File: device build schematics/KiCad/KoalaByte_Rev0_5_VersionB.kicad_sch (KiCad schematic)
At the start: 0 parts

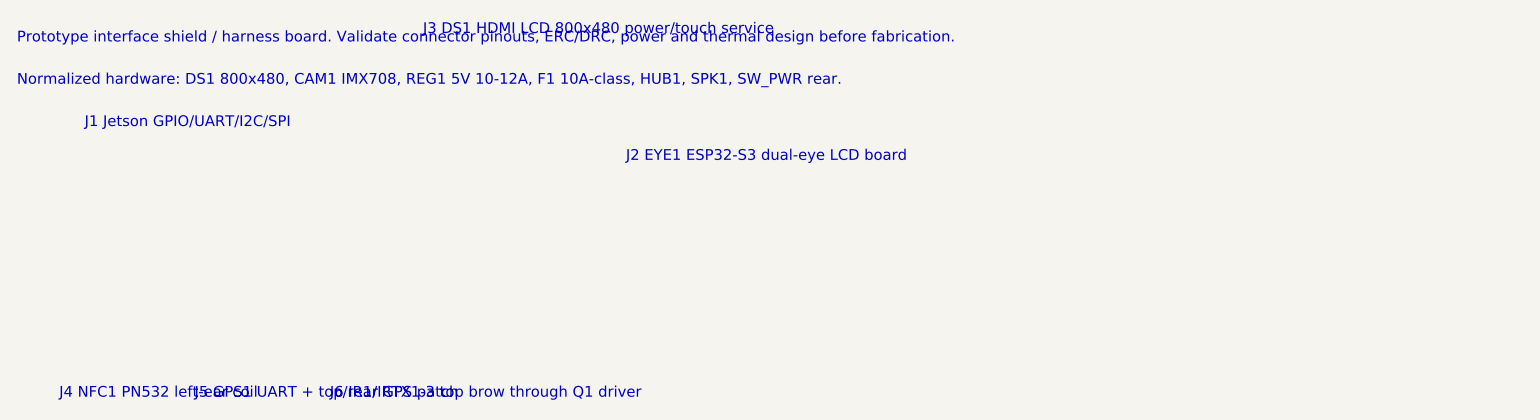
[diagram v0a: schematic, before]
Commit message: Add MIC1 schematic starter annotation
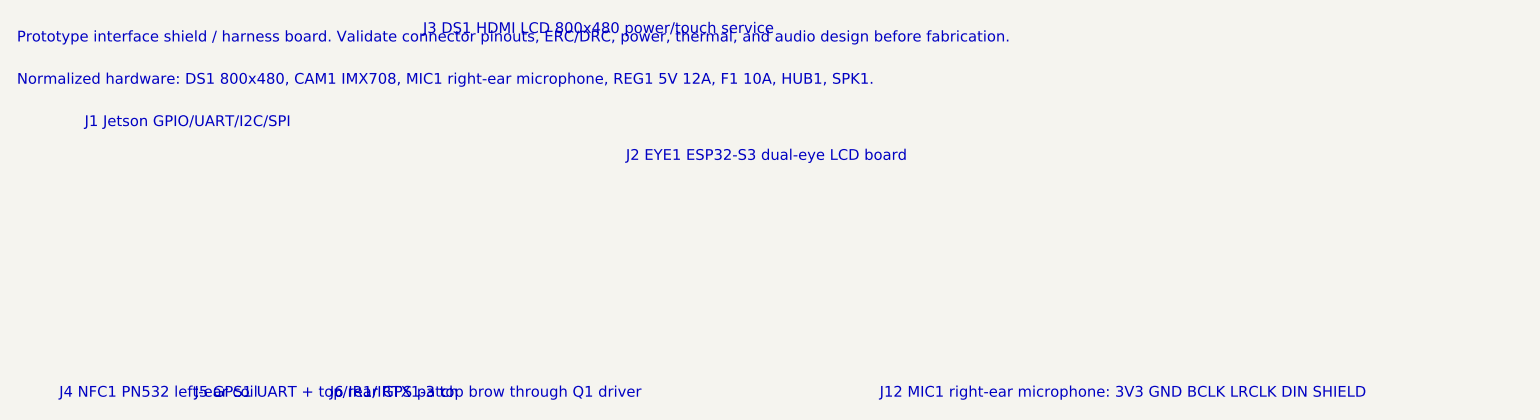
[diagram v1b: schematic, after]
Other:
- note added: "J12 MIC1 right-ear microphone: 3V3 GND BCLK LRCLK DIN SHIELD"
- note added: "Normalized hardware: DS1 800x480, CAM1 IMX708, MIC1 right-ear microphone, REG1 5V 12A, F1 10A, HUB1, SPK1."
- note added: "Prototype interface shield / harness board. Validate connector pinouts, ERC/DRC, power, thermal, and audio design before fabrication."
- note removed: "Normalized hardware: DS1 800x480, CAM1 IMX708, REG1 5V 10-12A, F1 10A-class, HUB1, SPK1, SW_PWR rear."
- note removed: "Prototype interface shield / harness board. Validate connector pinouts, ERC/DRC, power and thermal design before fabrication."
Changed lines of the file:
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@@
     (rev "0.5B-normalized")
     (company "Urban Poacher / Koalabyte")
-    (comment 1 "CAM1 IMX708 nose-pod CSI camera; DS1 800x480 HDMI display")
-    (comment 2 "REG1 5V 10-12A; F1 10A-class protection; REG2 3V3 logic")
-    (comment 3 "EYE1 ESP32-S3 dual 1.28in IPS LCD board; HUB1 and SPK1 retained")
+    (comment 1 "CAM1 IMX708 centered above eyes; DS1 800x480 HDMI display")
+    (comment 2 "MIC1 right-ear microphone via J12 harness; SPK1 retained")
+    (comment 3 "REG1 5V 12A; F1 10A-class protection; REG2 3V3 logic")
   )
-  (text "Prototype interface shield / harness board. Validate connector pinouts, ERC/DRC, power and thermal design before fabrication." (at 10 10 0)
+  (text "Prototype interface shield / harness board. Validate connector pinouts, ERC/DRC, power, thermal, and audio design before fabrication." (at 10 10 0)
     (effects (font (size 1.27 1.27)) (justify left bottom))
   )
-  (text "Normalized hardware: DS1 800x480, CAM1 IMX708, REG1 5V 10-12A, F1 10A-class, HUB1, SPK1, SW_PWR rear." (at 10 15 0)
+  (text "Normalized hardware: DS1 800x480, CAM1 IMX708, MIC1 right-ear microphone, REG1 5V 12A, F1 10A, HUB1, SPK1." (at 10 15 0)
     (effects (font (size 1.27 1.27)) (justify left bottom))
   )
@@
   (text "J5 GPS1 UART + top/rear GPS patch" (at 31 52 0) (effects (font (size 1.27 1.27)) (justify left bottom)))
   (text "J6 IR1/IRTX1-3 top brow through Q1 driver" (at 47 52 0) (effects (font (size 1.27 1.27)) (justify left bottom)))
+  (text "J12 MIC1 right-ear microphone: 3V3 GND BCLK LRCLK DIN SHIELD" (at 112 52 0) (effects (font (size 1.27 1.27)) (justify left bottom)))
   (sheet_instances (path "/" (page "1")))
 )
